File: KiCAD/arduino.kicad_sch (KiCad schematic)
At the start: 1 part, among them U2 Metro_ESP32S3

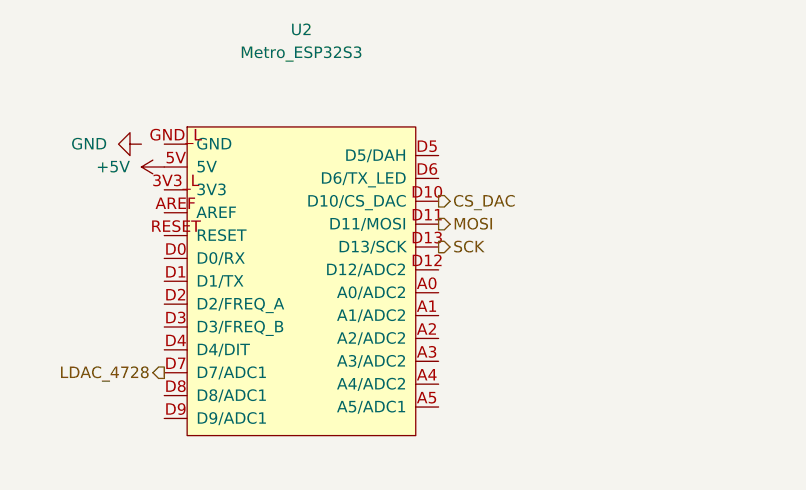
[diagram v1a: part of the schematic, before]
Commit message: kicad+pdf+tools: diode-OR build-out, cap footprints, regen monitor PDF
KiCad bias sheet: complete the cathode-monitor diode-OR combiner
  - D5, D6 = 1N4148 (diode-OR anodes at each LM393 OC output)
  - R24 = 100 kOhm (R_PD pulldown at common GRID_BLOCK_CRASH node)
  - R25 = 4.7 kOhm (second R_PULL so each LM393 OC has its own
    pull-up to +3.3 V, satisfying the diode-OR topology)
  - Closes the "remaining bias-sheet work" item from the cathode-
    monitor spec's open list.

KiCad arduino sheet: add I_CATHODE_A and I_CATHODE_B hierarchical
inputs so the ADC1 path from the bias sheet has a landing point on
the Metro side.

Tools: add assign_cap_footprints.py, a re-runnable script that walks
.kicad_sch files and assigns THT capacitor footprints by value, based
on the parts on the 2026-06-19 Mouser order:
  100nF / 0.1uF  KEMET C410   C_Disc_D5.0mm_W2.5mm_P5.00mm
  10uF           Panasonic    CP_Radial_D5.0mm_P2.00mm
  680nF / 0.68uF WIMA MKP4    C_Rect_L13.0mm_W6.0mm_P10.00mm_FKS3_FKP3_MKS4
  10nF / 0.01uF  Vishay Y5P   C_Disc_D6.0mm_W2.5mm_P5.00mm
  220pF          Knowles mica C_Rect_L7.0mm_W4.5mm_P5.00mm
Only fills empty Footprint fields; never overwrites. Preserves LF
line endings and writes UTF-8 without BOM (KiCad 10 treats a BOM-
prefixed .kicad_sch as empty).

Run output: 10 caps updated on bias sheet, 17 on buffer_keyer sheet.
Values still needing the user to measure (not in this order):
  bias: C17/C18 1uF, C21 0.22uF, C28/C29 1nF
  buffer_keyer: C1 330pF, C13/C14/C15 1uF
  vfo: CF3/CF5 390pF

Cathode_Monitor_Schematic.pdf regenerated with the diode-OR topology
locked in:
  - Schematic page adds L5b diode-OR sub-diagram (D_OR_A horizontal,
    D_OR_B from "Ch. B" annotation, R_PD pulldown, GRID_BLOCK_CRASH
    output)
  - R_SOURCE now drawn explicitly between OPA1641 OUT and LM393 (+)
  - V_REF block replaced with V_THR (R17/RV1/R18 trim, 1.06-2.13 V)
  - BOM, layers table, operating-points action column updated
  - "Watchdog gate" section rewritten: bias s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
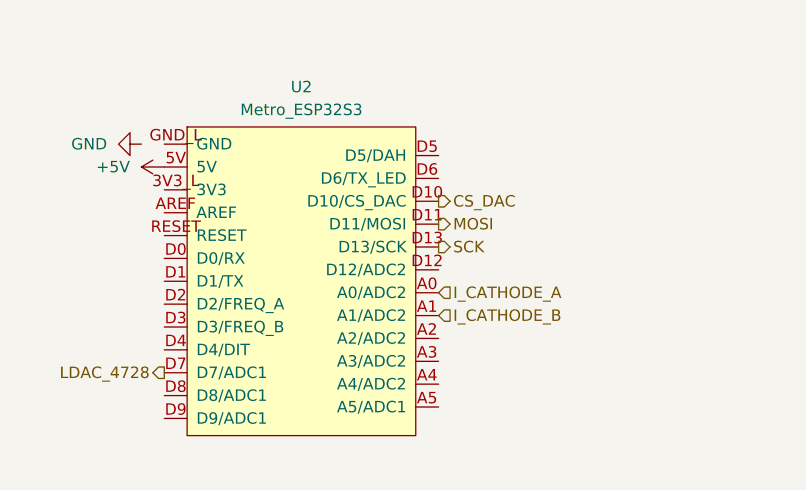
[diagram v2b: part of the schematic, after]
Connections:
- net I_CATHODE_A: now reaches U2.A0 (A0/ADC2)
- net I_CATHODE_B: now reaches U2.A1 (A1/ADC2)
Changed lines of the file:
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@@
+		)
+	)
+	(hierarchical_label "I_CATHODE_B"
+		(shape input)
+		(at 119.38 77.47 0)
+		(effects
+			(font
+				(size 1.27 1.27)
+			)
+			(justify left)
 		)
 	)
@@
 		(shape output)
 		(at 119.38 69.85 0)
+		(effects
+			(font
+				(size 1.27 1.27)
+			)
+			(justify left)
+		)
+	)
+	(hierarchical_label "I_CATHODE_A"
+		(shape input)
+		(at 119.38 74.93 0)
 		(effects
 			(font
@@
 		(fields_autoplaced yes)
 		(property "Reference" "U2"
-			(at 104.14 45.72 0)
+			(at 104.14 52.07 0)
 			(show_name no)
 			(do_not_autoplace no)
@@
 		)
 		(property "Value" "Metro_ESP32S3"
-			(at 104.14 48.26 0)
+			(at 104.14 54.61 0)
 			(show_name no)
 			(do_not_autoplace no)

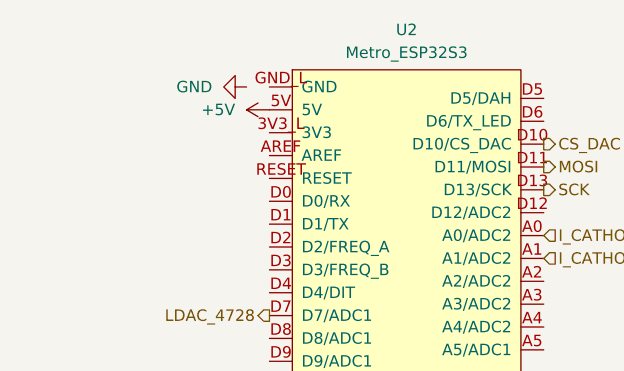
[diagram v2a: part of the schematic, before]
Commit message: front-panel: QT encoder swap, PCF8575 breakout, pre-fab checklist, INT-none decision
Switch STEP + FUNC from direct PCF8575 GPIO to Adafruit I2C QT Rotary
Encoder breakouts (PID 4991) at addr 0x36 / 0x37. The onboard seesaw
SAMD09 handles quadrature decoding + button debounce, dropping ~200
lines of firmware. PCF8575 still covers the LCD (4-bit), paddle, and
panel LEDs.

Add custom KiCad symbols + footprints for both new breakouts to
xmitter.kicad_sym and xmitter.pretty. Footprint properties on the new
symbols are pre-linked, so schematic instances auto-associate. Some
coordinates in both footprints are best-guess pending physical
measurement -- flagged in the descr fields and in the new
front_panel_interface.md open-items subsections.

Decision documented (2026-07-03): no INT wiring back to the Metro.
Firmware polls all three I2C devices at 100 Hz; velocity-adaptive VFO
tuning is computed from delta-position / delta-time in the poll loop.
Rationale and a "here's how to add INT later" path in the new
"Interrupt handling (decision: none)" section of
front_panel_interface.md.

New Documentation/pcb_fab_checklist.md is the consolidated pre-flight
gate before analog-board gerbers ship -- nine sections covering
footprint verification, schematic completeness, ERC/DRC, physical, and
BOM sign-offs. build_checklist.md and CLAUDE.md updated to point at it.

Also in this bundle: SDA/SCL hierarchical labels changed to
bidirectional shape on the VFO, buffer_keyer, and interface sheets
(was an output/input polarity soup that would have failed ERC).
Interface and Front_Panel child sheets registered in .kicad_pro.
Front_Panel is an empty stub; components go in when the sheet is
populated. Adafruit PCF8575 and QT rotary encoder datasheets committed
under Documentation/Components/.

Co-Authored-By: Claude Opus 4.7 <noreply@anthropic.com>
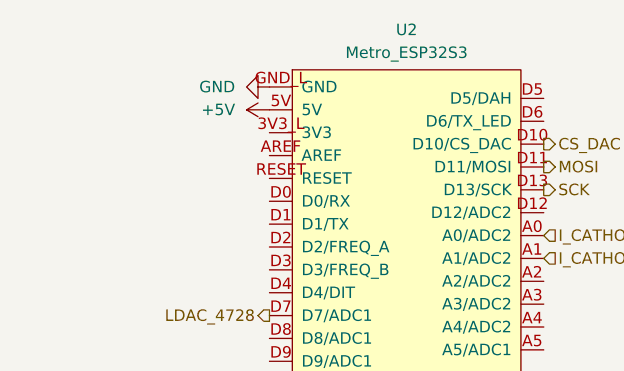
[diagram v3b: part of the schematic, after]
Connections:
- net GND: now also U2.GND_L (GND)
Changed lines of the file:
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@@
 	(symbol
 		(lib_id "power:GND")
-		(at 86.36 58.42 270)
+		(at 88.9 58.42 270)
 		(unit 1)
 		(body_style 1)
@@
 		(fields_autoplaced yes)
 		(property "Reference" "#PWR021"
-			(at 80.01 58.42 0)
+			(at 82.55 58.42 0)
 			(hide yes)
 			(show_name no)
@@
 		)
 		(property "Value" "GND"
-			(at 82.55 58.4199 90)
+			(at 85.09 58.4199 90)
 			(show_name no)
 			(do_not_autoplace no)
@@
 		)
 		(property "Footprint" ""
-			(at 86.36 58.42 0)
+			(at 88.9 58.42 0)
 			(hide yes)
 			(show_name no)
@@
 		)
 		(property "Datasheet" ""
-			(at 86.36 58.42 0)
+			(at 88.9 58.42 0)
 			(hide yes)
 			(show_name no)
@@
 		)
 		(property "Description" "Power symbol creates a global label with name \"GND\" , ground"
-			(at 86.36 58.42 0)
+			(at 88.9 58.42 0)
 			(hide yes)
 			(show_name no)

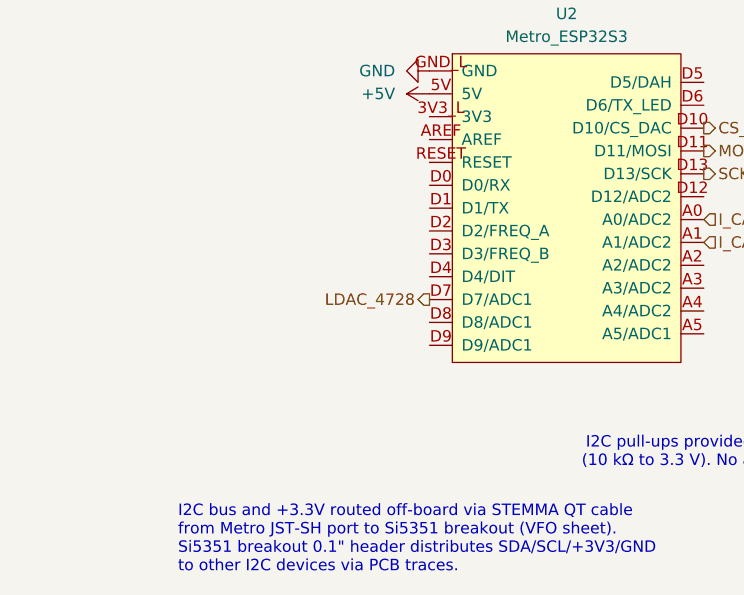
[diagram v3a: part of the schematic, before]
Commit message: arduino: reserve D4 for future ENC_INT + AM26LS32A datasheet
Add hardware provisions to arduino.kicad_sch for a possible future
front-panel interrupt cable, without committing to actually running one
on this build:

- Metro D4 (was D4/DIT; free since paddle moved to PCF8575) reserved
  as ENC_INT input
- R102 = 10 kOhm pull-up from D4 to +3.3V so the pin idles high with
  no cable connected
- J50 = 2-pin 0.1" header (ENC_INT_CABLE), footprint
  PinHeader_1x02_P2.54mm_Vertical. Leave unpopulated on first build
- Plain "ENC_INT" net label + text note explaining the reservation

If we ever want the INT cable later, it's a solder-in-a-header + run
a-cable operation with no PCB respin. Firmware sees D4 as a normal
edge-triggered input; external 10K means no internal pull-up needed.

Doc update: renamed the front_panel_interface.md "Interrupt handling"
section header from "(decision: none)" to "(decision: polling now, INT
hardware reserved)" and added the pin/component reservation list.

Also committing Documentation/Components/am26ls32a.pdf -- the TI
AM26LS32A datasheet for the RS-422 receiver going in the next Mouser
cart.

Co-Authored-By: Claude Opus 4.7 <noreply@anthropic.com>
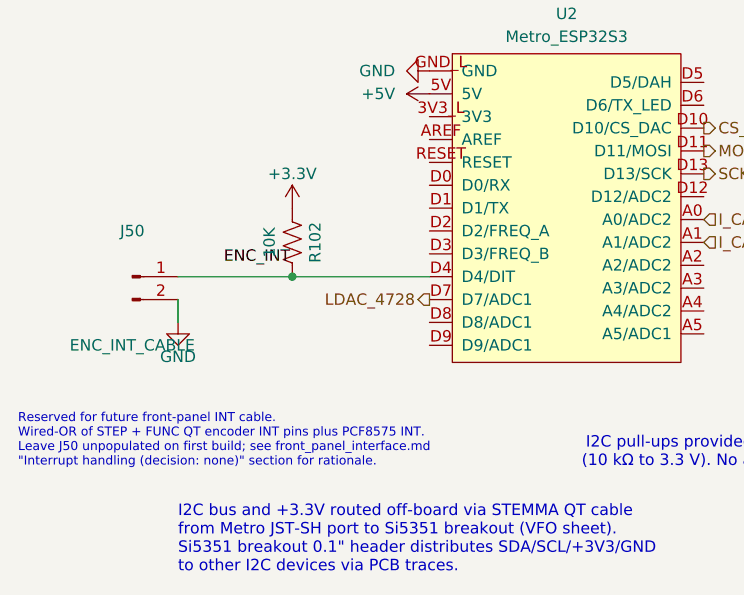
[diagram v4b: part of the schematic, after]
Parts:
- added J50: ENC_INT_CABLE, Connector_PinHeader_2.54mm:PinHeader_1x02_P2.54mm_Vertical, symbol Connector:Conn_01x02_Pin
- added R102: 10K, Resistor_THT:R_Axial_DIN0207_L6.3mm_D2.5mm_P10.16mm_Horizontal, symbol Device:R_US
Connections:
- net GND: now also J50.2 (Pin_2)
- net at U2.D4 (D4/DIT): now also J50.1 (Pin_1), R102.2
- new net +3.3V: R102.1
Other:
- note added: "Reserved for future front-panel INT cable. Wired-OR of STEP + FUNC QT encoder INT pins plus PCF8575 INT. Leave J50 unpopulated on first build; see front_panel_interface.md "Interrupt handling (decision: none)" section for rationale."

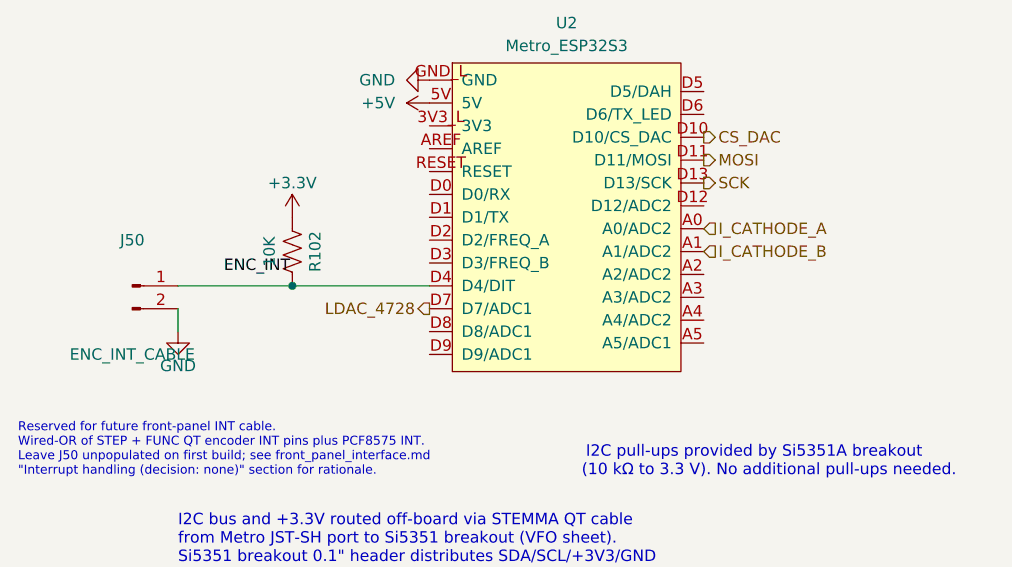
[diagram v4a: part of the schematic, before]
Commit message: interface+arduino: wire the MBL-600 signal chain end-to-end
Interface sheet — receiver + termination + level-shift, all live:
  - RJ45 J1 (shielded 8P8C, Connector library symbol) instantiated with
    hierarchical labels on all eight positions per T568B; RJ45 pins
    3/6/7/8 land on MBL_A_P/N and MBL_B_P/N at the receiver-input side
  - R100 = R101 = 120 Ohm across the differential pairs (RS-422
    termination at the receiver end)
  - AM26LS32ACN (U15) at (119.38, 104.14); ch 1 handles MBL_A±, ch 2
    handles MBL_B±
  - Both enable pins tied to GND. ~G at pin 4 is the active-LOW
    enable, so GND puts it in its active state and turns on all four
    receivers per the datasheet's OR-logic gate (the other enable at
    pin 12 stays inactive at GND, but that is fine -- either one active
    is enough). GND was chosen over VCC purely for routing ease --
    GND fill will be closer than +5V traces at layout time
  - 2.2K + 10K voltage divider on each channel output (R26+R28 for A,
    R27+R29 for B). Ratio 10/12.2 = 0.82 drops the ~3.4 V TTL to
    ~2.79 V at the divider midpoint, comfortably below the ESP32
    absolute-max of 3.6 V and comfortably above V_IH_min (~2.475 V)
  - MBL600_A and MBL600_B hierarchical labels attached at the divider
    midpoints (not at the receiver 1Y/2Y pins) so the divided signal is
    what leaves the sheet
  - VCC (pin 16) wired to +5V, bypassed by 10 uF electrolytic + 100 nF
    ceramic (datasheet requires only 0.1 uF minimum; the 10 uF is
    just bonus bulk)
  - Unused channels 3&4 A/B inputs and 3Y/4Y outputs left unconnected
    per datasheet allowance

Arduino sheet:
  - MBL600_A hierarchical label at Metro D2, MBL600_B at Metro D3 --
    matches the FREQ_A / FREQ_B slots that the Metro symbol reserved
  - I_CATHODE_A moved from A0 (ADC2) to D8 (ADC1)
  - I_CATHODE_B moved from A1 (ADC2) to D9 (ADC1) -- both now on ADC1
    per the cathode-monitor design decision; the old A0/A1 assignment
    would have conflicted with WiFi/BL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
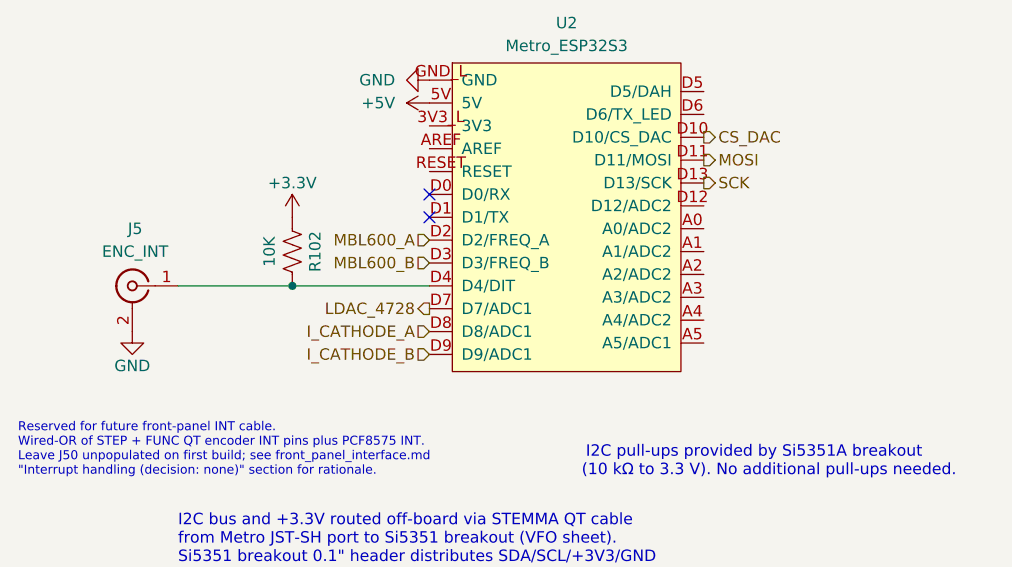
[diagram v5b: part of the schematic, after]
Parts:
- removed J50: ENC_INT_CABLE, Connector_PinHeader_2.54mm:PinHeader_1x02_P2.54mm_Vertical, symbol Connector:Conn_01x02_Pin
- added J5: ENC_INT, symbol Connector:Conn_Coaxial
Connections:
- net GND: now also J5.2 (Ext)
- net I_CATHODE_A: now also U2.D8 (D8/ADC1); no longer U2.A0 (A0/ADC2)
- net I_CATHODE_B: now also U2.D9 (D9/ADC1); no longer U2.A1 (A1/ADC2)
- net MBL600_A: now reaches U2.D2 (D2/FREQ_A)
- net MBL600_B: now reaches U2.D3 (D3/FREQ_B)
- net at R102.2, U2.D4 (D4/DIT): now also J5.1 (In)
- no-connect marks 0 -> 2

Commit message: kicad: SameSky RCJ-02 RCA jack footprint + link to J5 on arduino sheet
New custom footprint at xmitter.pretty/SameSky_RCJ-02_RCA_Jack.kicad_mod
matching the datasheet page-2 PCB layout: one 1.70 mm signal hole at
origin (pad 1 = center pin), two 2.00 mm mounting-foot holes at
(+/-5.15, +1.60) mm sharing pad number 2 (both mounting feet connect
to the shield/GND net). Silkscreen and fab layers show the connector
body outline plus a barrel circle indicating the opening direction
(faces -Y).

Assigned to J5 on arduino.kicad_sch -- the Conn_Coaxial symbol the user
placed for the future front-panel INT cable landing. Pin-number
convention matches (Conn_Coaxial pin 1 = center/signal, pin 2 = shield),
so no CvPcb intervention needed.

Co-Authored-By: Claude Opus 4.7 <noreply@anthropic.com>
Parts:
- J5: footprint (none) -> xmitter:SameSky_RCJ-02_RCA_Jack
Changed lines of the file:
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@@
 			)
 		)
-		(property "Footprint" ""
+		(property "Footprint" "xmitter:SameSky_RCJ-02_RCA_Jack"
 			(at 55.88 81.28 0)
 			(hide yes)
